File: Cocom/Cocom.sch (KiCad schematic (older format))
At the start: 15 parts

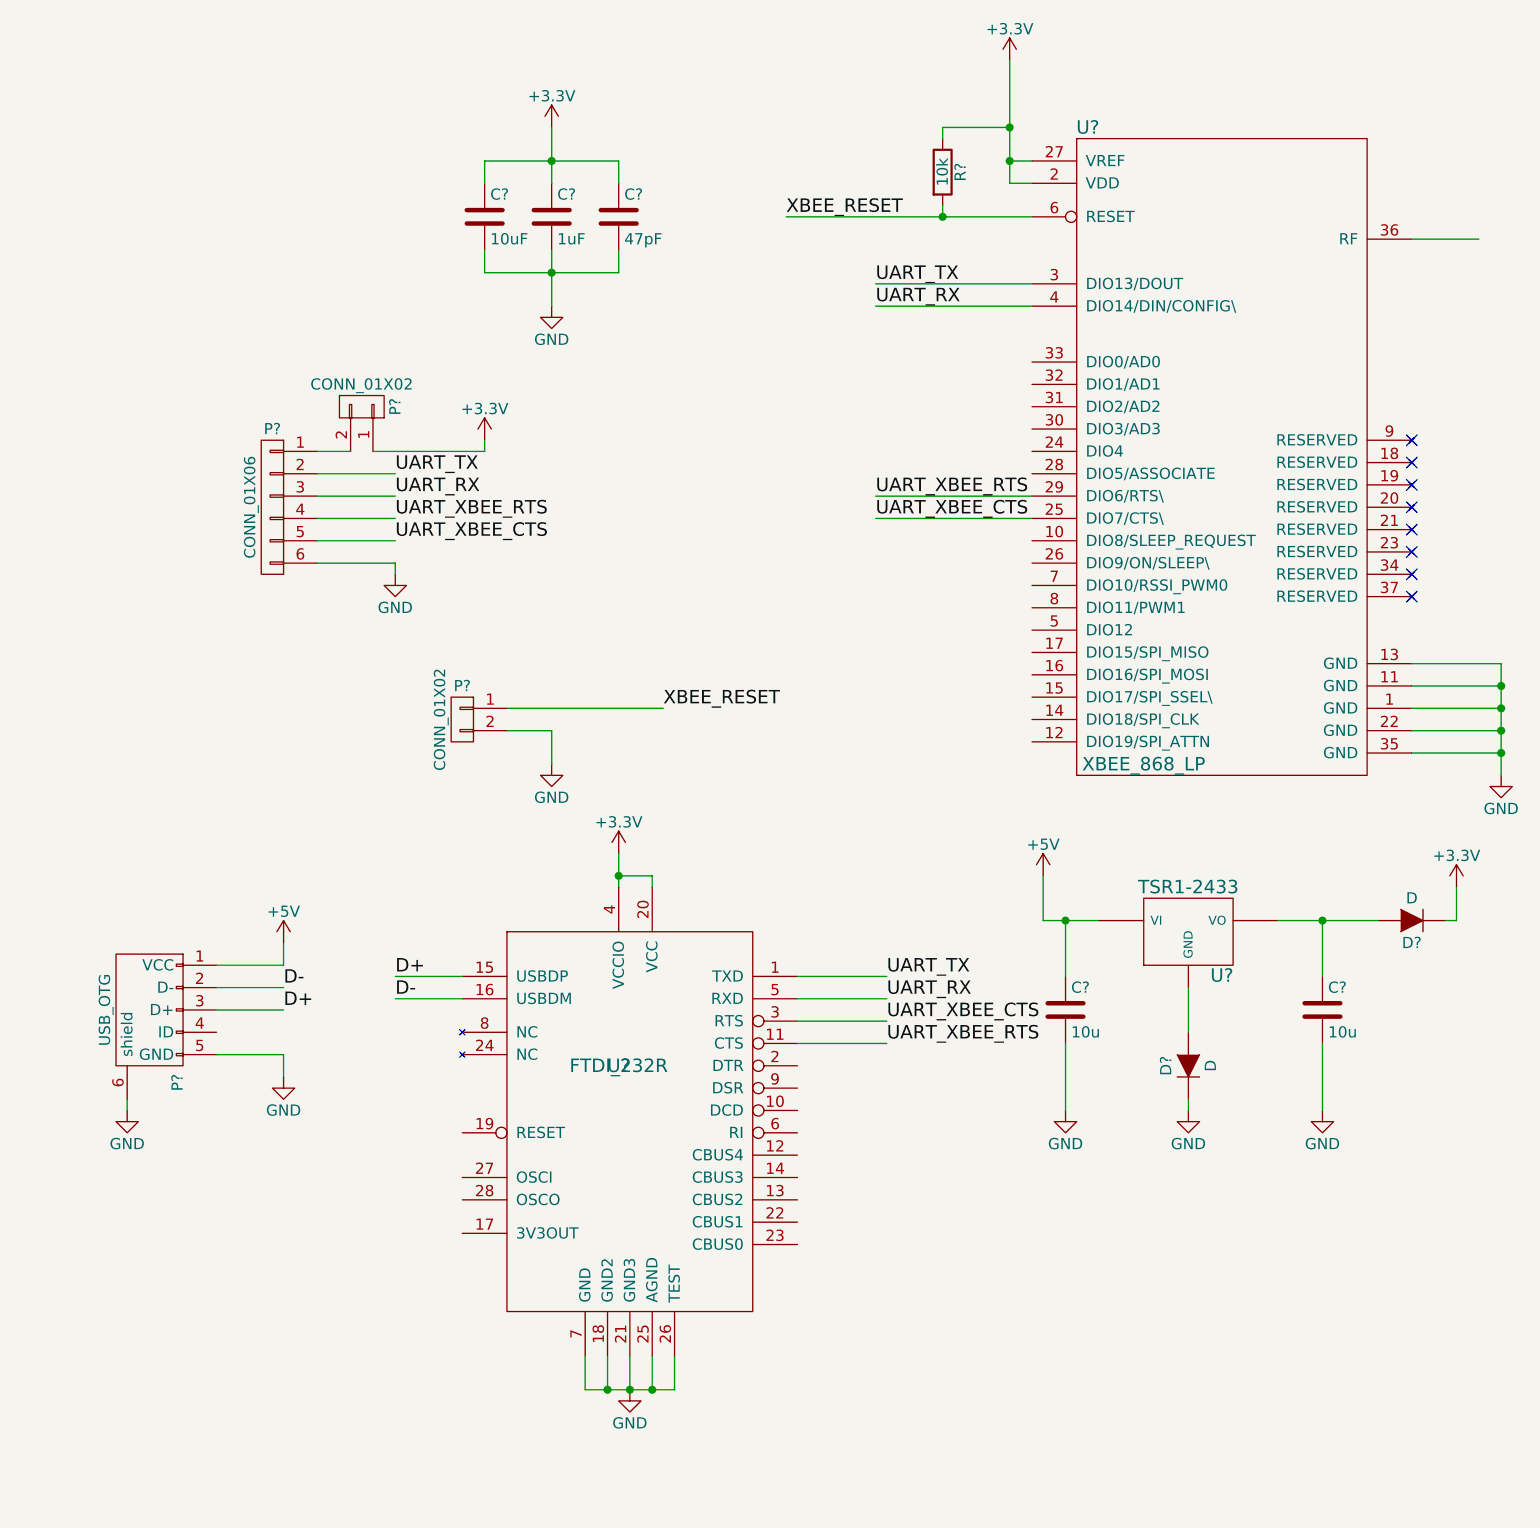
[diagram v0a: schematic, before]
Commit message: Add led for com
Rajout des leds du FTDI
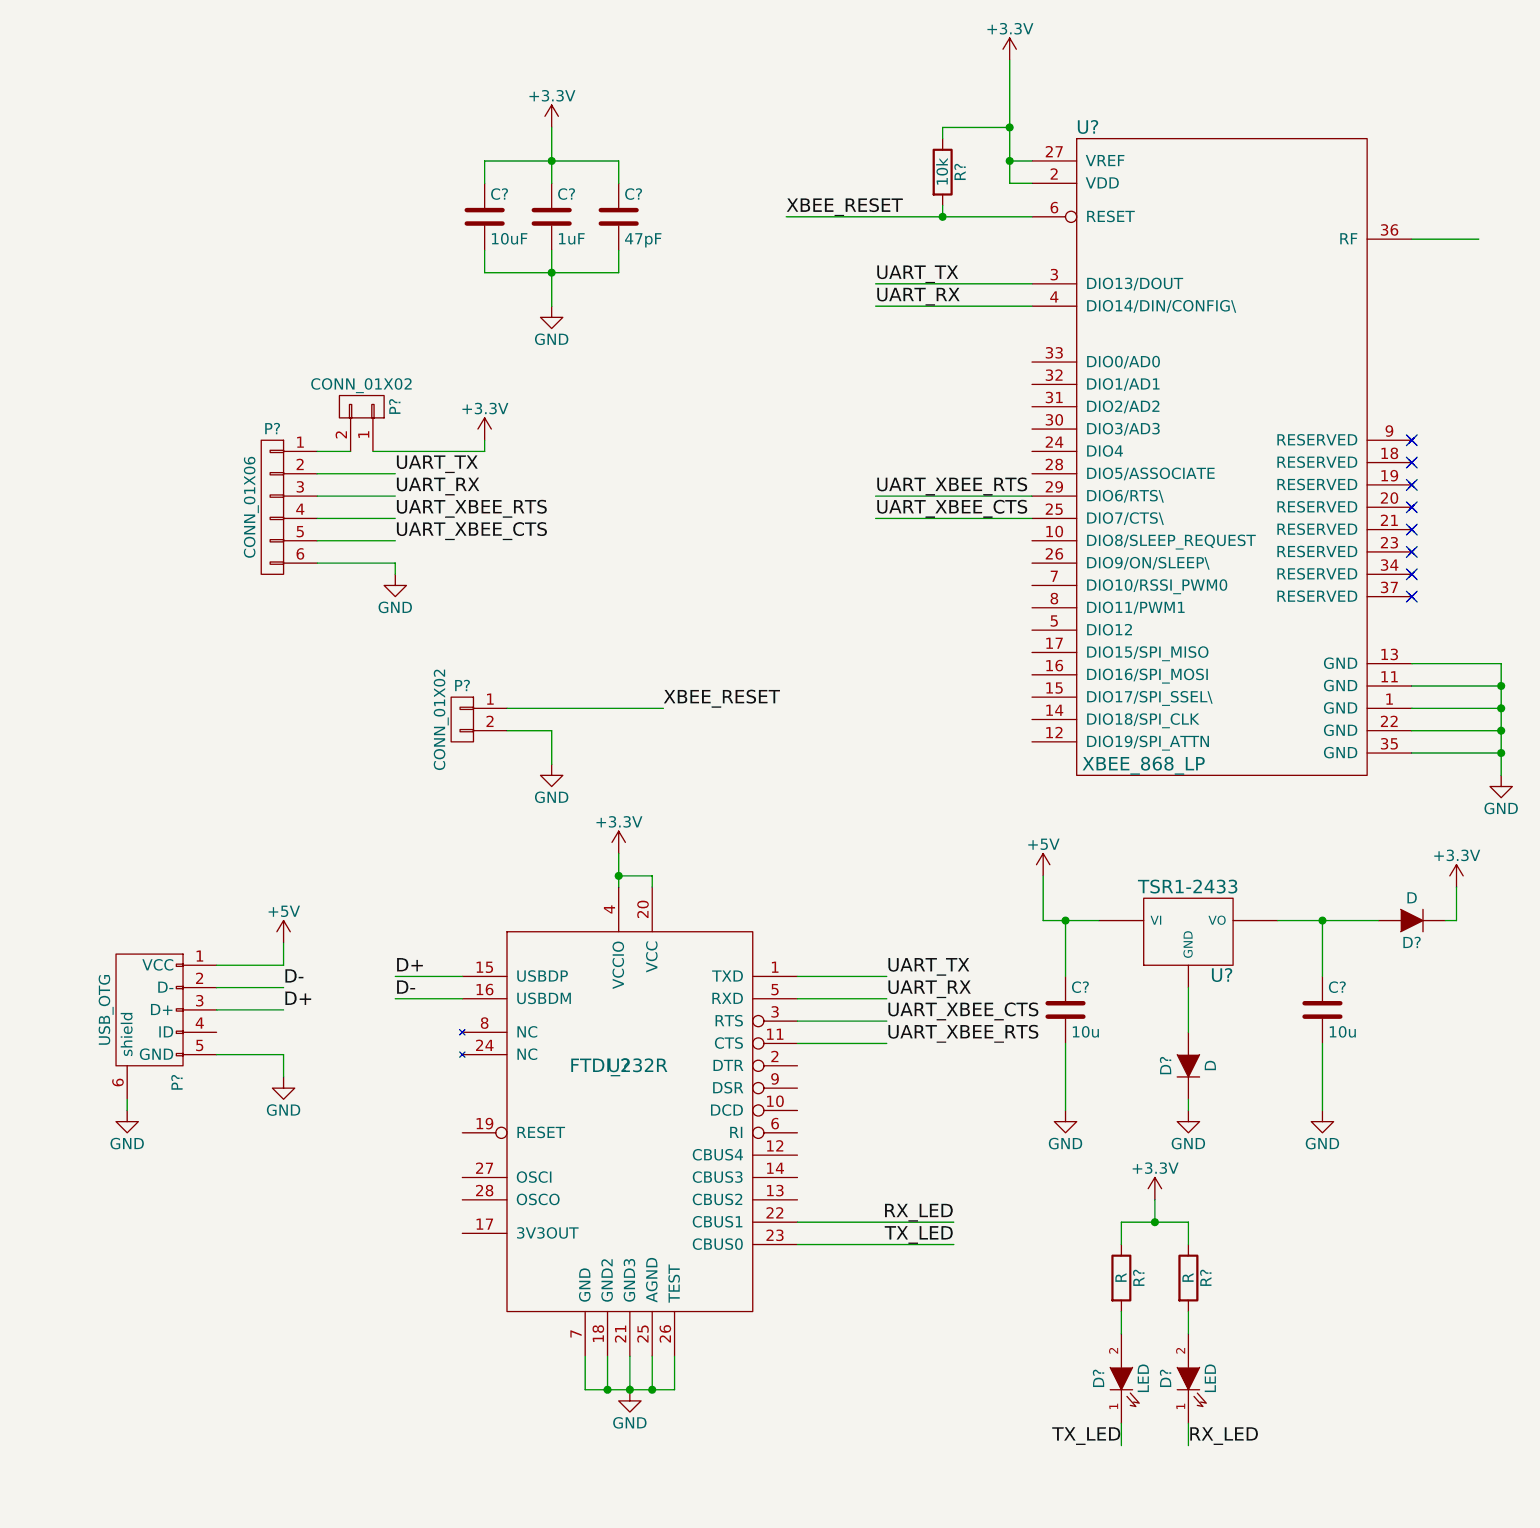
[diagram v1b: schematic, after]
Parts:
- added D? (x2): LED, symbol LED
- added R? (x2): R, symbol R
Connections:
- net +3V3: now also R?.1, R?.1
- net RX_LED: now reaches U?.22 (CBUS1)
- net RX_LED: now also D?.1 (K)
- net TX_LED: now reaches U?.23 (CBUS0)
- net TX_LED: now also D?.1 (K)
- new net: D?.2 (A), R?.2 (x2)
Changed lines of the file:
@@
 	0    -1   -1   0
 $EndComp
-Wire Wire Line
-	4700 1800 4800 1800
-Wire Wire Line
-	4700 1900 4800 1900
-Wire Wire Line
-	4700 1350 4700 1650
-Wire Wire Line
-	4700 1650 4700 1800
-Wire Wire Line
-	4700 1800 4700 1900
-Connection ~ 4700 1800
-Connection ~ 4700 1650
-Wire Wire Line
-	6900 4050 6900 4150
-Wire Wire Line
-	6900 4150 6900 4250
-Wire Wire Line
-	6900 4250 6900 4350
-Wire Wire Line
-	6900 4350 6900 4450
-Wire Wire Line
-	6900 4450 6900 4550
-Wire Wire Line
-	6900 4050 6500 4050
-Wire Wire Line
-	6500 4150 6900 4150
-Connection ~ 6900 4150
-Wire Wire Line
-	6500 4250 6900 4250
-Connection ~ 6900 4250
-Wire Wire Line
-	6500 4350 6900 4350
-Connection ~ 6900 4350
-Wire Wire Line
-	6500 4450 6900 4450
-Connection ~ 6900 4450
-Wire Wire Line
-	4800 2350 4100 2350
-Wire Wire Line
-	4800 2450 4100 2450
-Wire Wire Line
-	2950 1800 2950 1900
-Wire Wire Line
-	2350 1800 2650 1800
-Wire Wire Line
-	2650 1800 2950 1800
-Wire Wire Line
-	2350 1800 2350 1900
-Wire Wire Line
-	2650 1650 2650 1800
-Wire Wire Line
-	2650 1800 2650 1900
-Connection ~ 2650 1800
-Wire Wire Line
-	2350 2200 2350 2300
-Wire Wire Line
-	2350 2300 2650 2300
-Wire Wire Line
-	2650 2300 2950 2300
-Wire Wire Line
-	2950 2300 2950 2200
-Wire Wire Line
-	2650 2200 2650 2300
-Wire Wire Line
-	2650 2300 2650 2450
-Connection ~ 2650 2300
-Wire Wire Line
-	4400 2000 4400 2050
-Wire Wire Line
-	4400 1700 4400 1650
-Wire Wire Line
-	4400 1650 4700 1650
-Wire Wire Line
-	3700 2050 4400 2050
-Wire Wire Line
-	4400 2050 4800 2050
-Wire Wire Line
-	4800 3300 4100 3300
-Wire Wire Line
-	4800 3400 4100 3400
-Wire Wire Line
-	6500 2150 6800 2150
-Wire Wire Line
-	2350 3100 2350 3050
-Wire Wire Line
-	1600 3200 1950 3200
-Wire Wire Line
-	1950 3300 1600 3300
-Wire Wire Line
-	1600 3400 1950 3400
-Wire Wire Line
-	1950 3500 1600 3500
-Wire Wire Line
-	1600 3600 1950 3600
-Wire Wire Line
-	1950 3600 1950 3650
-Wire Wire Line
-	2450 4350 2650 4350
-Wire Wire Line
-	2650 4350 2650 4500
-Wire Wire Line
-	2450 4250 3150 4250
-Connection ~ 4400 2050
-Wire Wire Line
-	4150 5450 3750 5450
-Wire Wire Line
-	3750 5550 4150 5550
-Wire Wire Line
-	1600 3100 1750 3100
-Wire Wire Line
-	1850 3100 2350 3100
-Wire Wire Line
-	3750 5650 4150 5650
-Wire Wire Line
-	4150 5750 3750 5750
-Wire Wire Line
-	5100 5200 4950 5200
-Wire Wire Line
-	4950 5200 4850 5200
-Wire Wire Line
-	4850 5200 4850 5000
-Wire Wire Line
-	5900 5200 6100 5200
-Wire Wire Line
-	6100 5200 6350 5200
-Wire Wire Line
-	5500 5500 5500 5700
-Wire Wire Line
-	6700 5200 6700 5050
-Wire Wire Line
-	4950 6050 4950 5750
-Wire Wire Line
-	6100 5750 6100 6050
-Wire Wire Line
-	2950 4900 2950 5000
-Wire Wire Line
-	2950 5000 2950 5050
-Wire Wire Line
-	3100 5050 3100 5000
-Wire Wire Line
-	3100 5000 2950 5000
-Connection ~ 2950 5000
-Wire Wire Line
-	2800 7150 2800 7300
-Wire Wire Line
-	2800 7300 2900 7300
-Wire Wire Line
-	2900 7300 3000 7300
-Wire Wire Line
-	3000 7300 3100 7300
-Wire Wire Line
-	3100 7300 3200 7300
-Wire Wire Line
-	2900 7150 2900 7300
-Connection ~ 2900 7300
-Wire Wire Line
-	3000 7300 3000 7150
-Wire Wire Line
-	3100 7300 3100 7150
-Connection ~ 3000 7300
-Wire Wire Line
-	3200 7300 3200 7150
-Connection ~ 3100 7300
-Wire Wire Line
-	1150 5600 1450 5600
-Wire Wire Line
-	1950 5450 2250 5450
-Wire Wire Line
-	1450 5500 1150 5500
-Wire Wire Line
-	1150 5400 1450 5400
-Wire Wire Line
-	1450 5400 1450 5300
-Wire Wire Line
-	1150 5800 1450 5800
-Wire Wire Line
-	1450 5800 1450 5900
-Wire Wire Line
-	1950 5550 2250 5550
-Wire Wire Line
-	750  6000 750  6050
-Wire Wire Line
-	6700 5200 6650 5200
-Wire Wire Line
-	5500 6000 5500 6050
-Wire Wire Line
-	6100 5450 6100 5200
-Connection ~ 6100 5200
-Wire Wire Line
-	4950 5450 4950 5200
-Connection ~ 4950 5200
 $Comp
 L CONN_01X02 P?
@@
 	0    1    -1   0
 $EndComp
+$Comp
+L R R?
+U 1 1 578C75BB
+P 5500 6800
+F 0 "R?" V 5580 6800 50  0000 C CNN
+F 1 "R" V 5500 6800 50  0000 C CNN
+F 2 "" V 5430 6800 50  0000 C CNN
+F 3 "" H 5500 6800 50  0000 C CNN
+	1    5500 6800
+	1    0    0    -1
+$EndComp
+$Comp
+L LED D?
+U 1 1 578C762C
+P 5500 7250
+F 0 "D?" H 5500 7350 50  0000 C CNN
+F 1 "LED" H 5500 7150 50  0000 C CNN
+F 2 "" H 5500 7250 50  0000 C CNN
+F 3 "" H 5500 7250 50  0000 C CNN
+	1    5500 7250
+	0    -1   -1   0
+$EndComp
+$Comp
+L R R?
+U 1 1 578C7A39
+P 5200 6800
+F 0 "R?" V 5280 6800 50  0000 C CNN
+F 1 "R" V 5200 6800 50  0000 C CNN
+F 2 "" V 5130 6800 50  0000 C CNN
+F 3 "" H 5200 6800 50  0000 C CNN
+	1    5200 6800
+	1    0    0    -1
+$EndComp
+$Comp
+L LED D?
+U 1 1 578C7A8F
+P 5200 7250
+F 0 "D?" H 5200 7350 50  0000 C CNN
+F 1 "LED" H 5200 7150 50  0000 C CNN
+F 2 "" H 5200 7250 50  0000 C CNN
+F 3 "" H 5200 7250 50  0000 C CNN
+	1    5200 7250
+	0    -1   -1   0
+$EndComp
+Wire Wire Line
+	4700 1800 4800 1800
+Wire Wire Line
+	4700 1900 4800 1900
+Wire Wire Line
+	4700 1350 4700 1900
+Connection ~ 4700 1800
+Connection ~ 4700 1650
+Wire Wire Line
+	6900 4050 6900 4550
+Wire Wire Line
+	6900 4050 6500 4050
+Wire Wire Line
+	6500 4150 6900 4150
+Connection ~ 6900 4150
+Wire Wire Line
+	6500 4250 6900 4250
+Connection ~ 6900 4250
+Wire Wire Line
+	6500 4350 6900 4350
+Connection ~ 6900 4350
+Wire Wire Line
+	6500 4450 6900 4450
+Connection ~ 6900 4450
+Wire Wire Line
+	4800 2350 4100 2350
+Wire Wire Line
+	4800 2450 4100 2450
+Wire Wire Line
+	2950 1800 2950 1900
+Wire Wire Line
+	2350 1800 2950 1800
+Wire Wire Line
+	2350 1800 2350 1900
+Wire Wire Line
+	2650 1650 2650 1900
+Connection ~ 2650 1800
+Wire Wire Line
+	2350 2200 2350 2300
+Wire Wire Line
+	2350 2300 2950 2300
+Wire Wire Line
+	2950 2300 2950 2200
+Wire Wire Line
+	2650 2200 2650 2450
+Connection ~ 2650 2300
+Wire Wire Line
+	4400 2000 4400 2050
+Wire Wire Line
+	4400 1700 4400 1650
+Wire Wire Line
+	4400 1650 4700 1650
+Wire Wire Line
+	3700 2050 4800 2050
+Wire Wire Line
+	4800 3300 4100 3300
+Wire Wire Line
+	4800 3400 4100 3400
+Wire Wire Line
+	6500 2150 6800 2150
+Wire Wire Line
+	2350 3100 2350 3050
+Wire Wire Line
+	1600 3200 1950 3200
+Wire Wire Line
+	1950 3300 1600 3300
+Wire Wire Line
+	1600 3400 1950 3400
+Wire Wire Line
+	1950 3500 1600 3500
+Wire Wire Line
+	1600 3600 1950 3600
+Wire Wire Line
+	1950 3600 1950 3650
+Wire Wire Line
+	2450 4350 2650 4350
+Wire Wire Line
+	2650 4350 2650 4500
+Wire Wire Line
+	2450 4250 3150 4250
+Connection ~ 4400 2050
+Wire Wire Line
+	4150 5450 3750 5450
+Wire Wire Line
+	3750 5550 4150 5550
+Wire Wire Line
+	1600 3100 1750 3100
+Wire Wire Line
+	1850 3100 2350 3100
+Wire Wire Line
+	3750 5650 4150 5650
+Wire Wire Line
+	4150 5750 3750 5750
+Wire Wire Line
+	4850 5200 5100 5200
+Wire Wire Line
+	4850 5200 4850 5000
+Wire Wire Line
+	5900 5200 6350 5200
+Wire Wire Line
+	5500 5500 5500 5700
+Wire Wire Line
+	6700 5200 6700 5050
+Wire Wire Line
+	4950 6050 4950 5750
+Wire Wire Line
+	6100 5750 6100 6050
+Wire Wire Line
+	2950 4900 2950 5050
+Wire Wire Line
+	3100 5050 3100 5000
+Wire Wire Line
+	3100 5000 2950 5000
+Connection ~ 2950 5000
+Wire Wire Line
+	2800 7150 2800 7300
+Wire Wire Line
+	2800 7300 3200 7300
+Wire Wire Line
+	2900 7150 2900 7300
+Connection ~ 2900 7300
+Wire Wire Line
+	3000 7300 3000 7150
+Wire Wire Line
+	3100 7300 3100 7150
+Connection ~ 3000 7300
+Wire Wire Line
+	3200 7300 3200 7150
+Connection ~ 3100 7300
+Wire Wire Line
+	1150 5600 1450 5600
+Wire Wire Line
+	1950 5450 2250 5450
+Wire Wire Line
+	1450 5500 1150 5500
+Wire Wire Line
+	1150 5400 1450 5400
+Wire Wire Line
+	1450 5400 1450 5300
+Wire Wire Line
+	1150 5800 1450 5800
+Wire Wire Line
+	1450 5800 1450 5900
+Wire Wire Line
+	1950 5550 2250 5550
+Wire Wire Line
+	750  6000 750  6050
+Wire Wire Line
+	6700 5200 6650 5200
+Wire Wire Line
+	5500 6000 5500 6050
+Wire Wire Line
+	6100 5450 6100 5200
+Connection ~ 6100 5200
+Wire Wire Line
+	4950 5450 4950 5200
+Connection ~ 4950 5200
+Wire Wire Line
+	5500 7550 5500 7450
+Wire Wire Line
+	5500 7050 5500 6950
+Wire Wire Line
+	5200 6650 5200 6550
+Wire Wire Line
+	5200 6550 5500 6550
+Wire Wire Line
+	5500 6550 5500 6650
+Wire Wire Line
+	5350 6450 5350 6550
+Connection ~ 5350 6550
+Wire Wire Line
+	5200 6950 5200 7050
+Wire Wire Line
+	5200 7450 5200 7550
+Text Label 5500 7550 0    60   ~ 0
+RX_LED
+Text Label 5200 7550 2    60   ~ 0
+TX_LED
+Text Label 4450 6650 2    60   ~ 0
+TX_LED
+Text Label 4450 6550 2    60   ~ 0
+RX_LED
+Wire Wire Line
+	3750 6550 4450 6550
+Wire Wire Line
+	3750 6650 4450 6650
+$Comp
+L +3.3V #PWR?
+U 1 1 578C8B6B
+P 5350 6450
+F 0 "#PWR?" H 5350 6300 50  0001 C CNN
+F 1 "+3.3V" H 5350 6590 50  0000 C CNN
+F 2 "" H 5350 6450 50  0000 C CNN
+F 3 "" H 5350 6450 50  0000 C CNN
+	1    5350 6450
+	1    0    0    -1
+$EndComp
 $EndSCHEMATC
